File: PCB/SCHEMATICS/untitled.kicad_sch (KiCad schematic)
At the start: 15 parts, among them Q1 NMOS, Q2 NPN, U1 LM7805_TO220, U2 AMS1117-3.3

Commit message: Updated Schematics
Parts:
- added D3: D_Schottky, symbol Device:D_Schottky
- added D4: D_Zener, symbol Device:D_Zener
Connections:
- net V3OUT is gone; now on net GND: C3.1, D1.2 (A), U2.2 (VO)
- net GND: now also D4.1 (K), D4.2 (A)
- net Vout: no longer names the net of C4.1, D1.1 (K), R2.1, U2.3 (VI)
- net Vout: now also D3.1 (K); no longer Q2.3 (E), R3.2
- net Vout1 renamed 5V TEST
- new net Vbatt: D3.2 (A), Q2.3 (E), R3.2

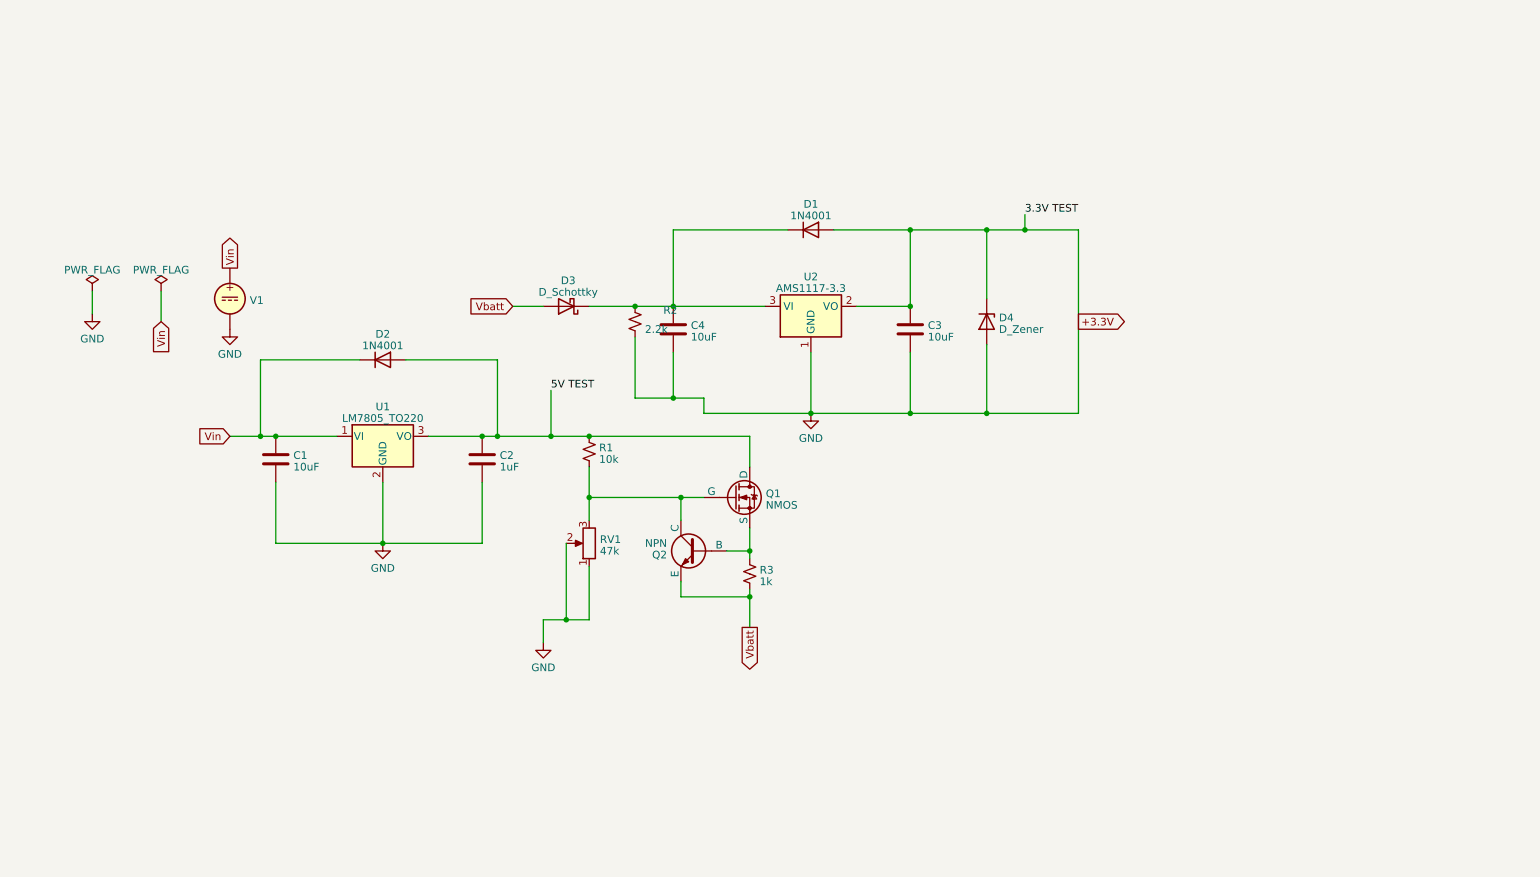
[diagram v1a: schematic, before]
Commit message: UPDATED SCHEMATICS.
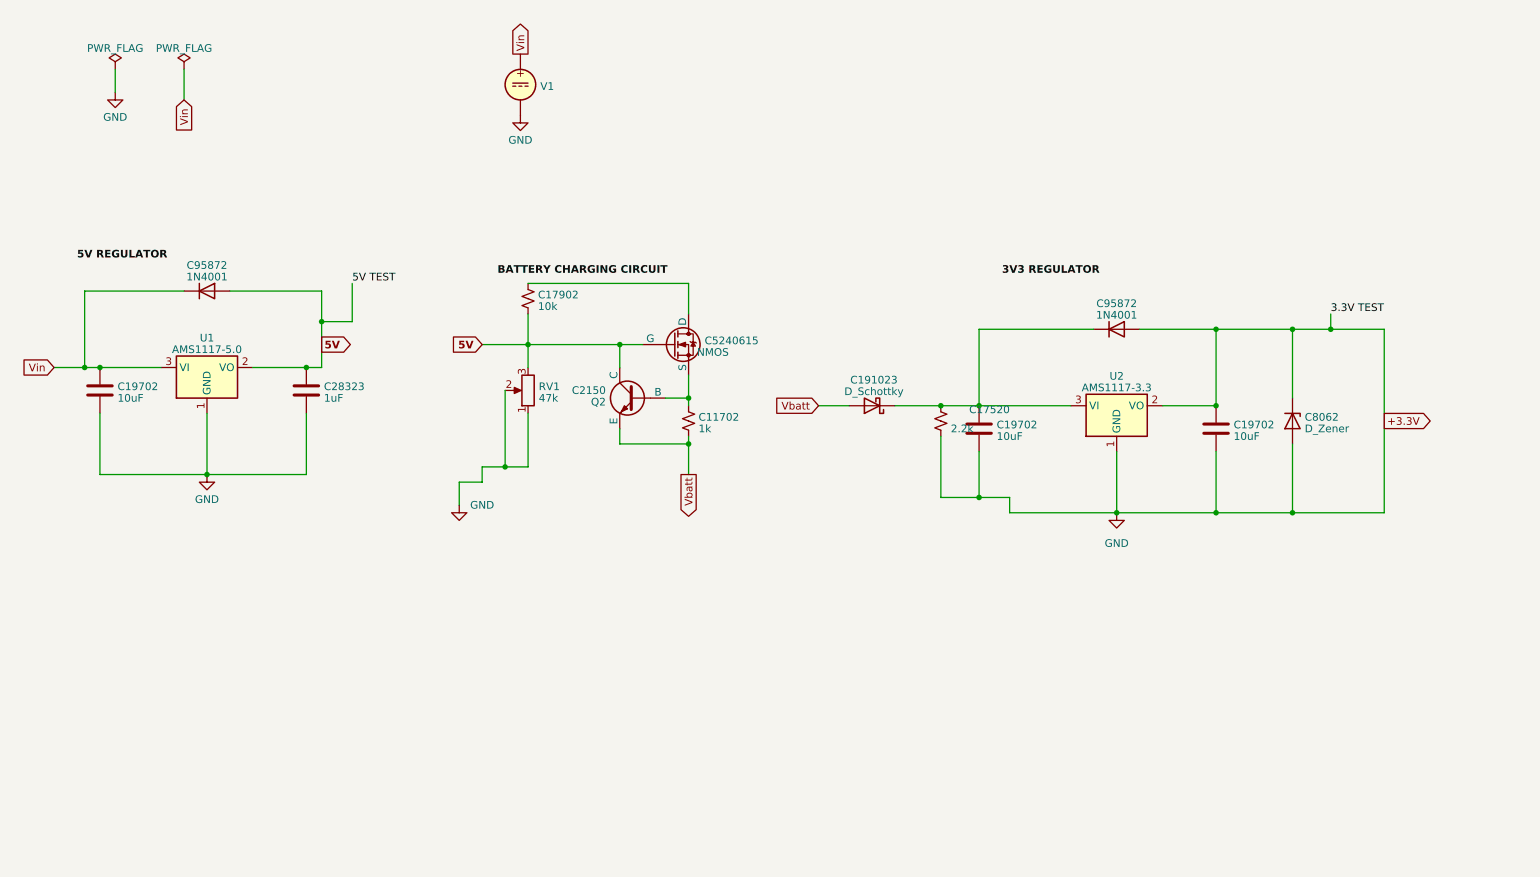
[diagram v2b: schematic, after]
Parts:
- removed U1: LM7805_TO220, Package_TO_SOT_THT:TO-220-3_Vertical, symbol Regulator_Linear:LM7805_TO220
- added U1: AMS1117-5.0, Package_TO_SOT_SMD:SOT-223-3_TabPin2, symbol Regulator_Linear:AMS1117-5.0
- C11702: renamed from R3; Unit Price (none) -> 0.0005
- C17520: renamed from R2; Unit Price (none) -> 0.0017
- C17902: renamed from R1; Unit Price (none) -> 0.003
- C191023: renamed from D3; Unit Price (none) -> 0.0167
- C19702: renamed from C1; Unit Price (none) -> 0.0066
- C19702: renamed from C3; Unit Price (none) -> 0.0066
- C19702: renamed from C4; Unit Price (none) -> 0.0066
- C28323: renamed from C2; Unit Price (none) -> 0.0087
- C5240615: renamed from Q1; Extended (none) -> YES; Unit Price (none) -> 0.0185
- C8062: renamed from D4; Unit Price (none) -> 0.0121
- C95872: renamed from D2; Unit Price (none) -> 0.0069
- C95872: renamed from D1; Unit Price (none) -> 0.0069
- Q2: value NPN -> C2150; Unit Price (none) -> 0.0147
- U2: Extended (none) -> YES; Unit Price (none) -> 0.0627
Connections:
- net GND: now also U1.1 (GND)
- net Vin: now also U1.3 (VI)
- net 5V: now reaches C17902.2, C5240615.2 (G), Q2.1 (C), RV1.3
- net 5V: now also C28323.1, C95872.2 (A), U1.2 (VO)
- net 5V TEST: no longer names the net of C17902.1, C5240615.1 (D)
- net 5V TEST: no longer C28323.1, C95872.2 (A)
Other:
- moved on the sheet: C11702, C17520, C17902, C191023, C19702, C28323, C5240615, C8062, C95872, Q2, RV1, U2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

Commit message: Updating schematics
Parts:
- removed C19702: 10uF, symbol Device:C
- removed C28323: 1uF, symbol Device:C
- removed C95872: 1N4001, Diode_THT:D_DO-41_SOD81_P10.16mm_Horizontal, symbol Diode:1N4001
- removed U1: AMS1117-5.0, Package_TO_SOT_SMD:SOT-223-3_TabPin2, symbol Regulator_Linear:AMS1117-5.0
- added C4: C_Small, symbol Device:C_Small
- added R1: R_Small_US, symbol Device:R_Small_US
- added TP3, TP4, TP5, TP6, TP7, TP8: TestPoint, symbol Connector:TestPoint
- added U1: ~, symbol Battery charging:TP4054
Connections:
- net 5V: now also TP3.1
- net GND: now also C4.2, R1.2, TP6.1, TP8.1, U1.1 (CHRG), U1.2 (GND)
- net Vbatt: now also TP4.1, TP5.1
- net at C17520.1, C191023.1 (K), C19702.1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: now also TP7.1
- new net: R1.1, U1.5 (Prog)
- new net Batt: U1.3 (BATT)
- new net USB: C4.1, U1.4 (Vcc)
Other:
- title: (none) -> POWER MODULE
- moved on the sheet: C11702, C17520, C17902, C5240615, Q2, RV1
